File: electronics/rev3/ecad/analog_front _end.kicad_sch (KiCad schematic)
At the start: 20 parts, among them J3 Red Banana Plug, J4 Black Banana Plug, SW3 GF-161-0005, U10 MCP3561, U3 OPA4388IDR

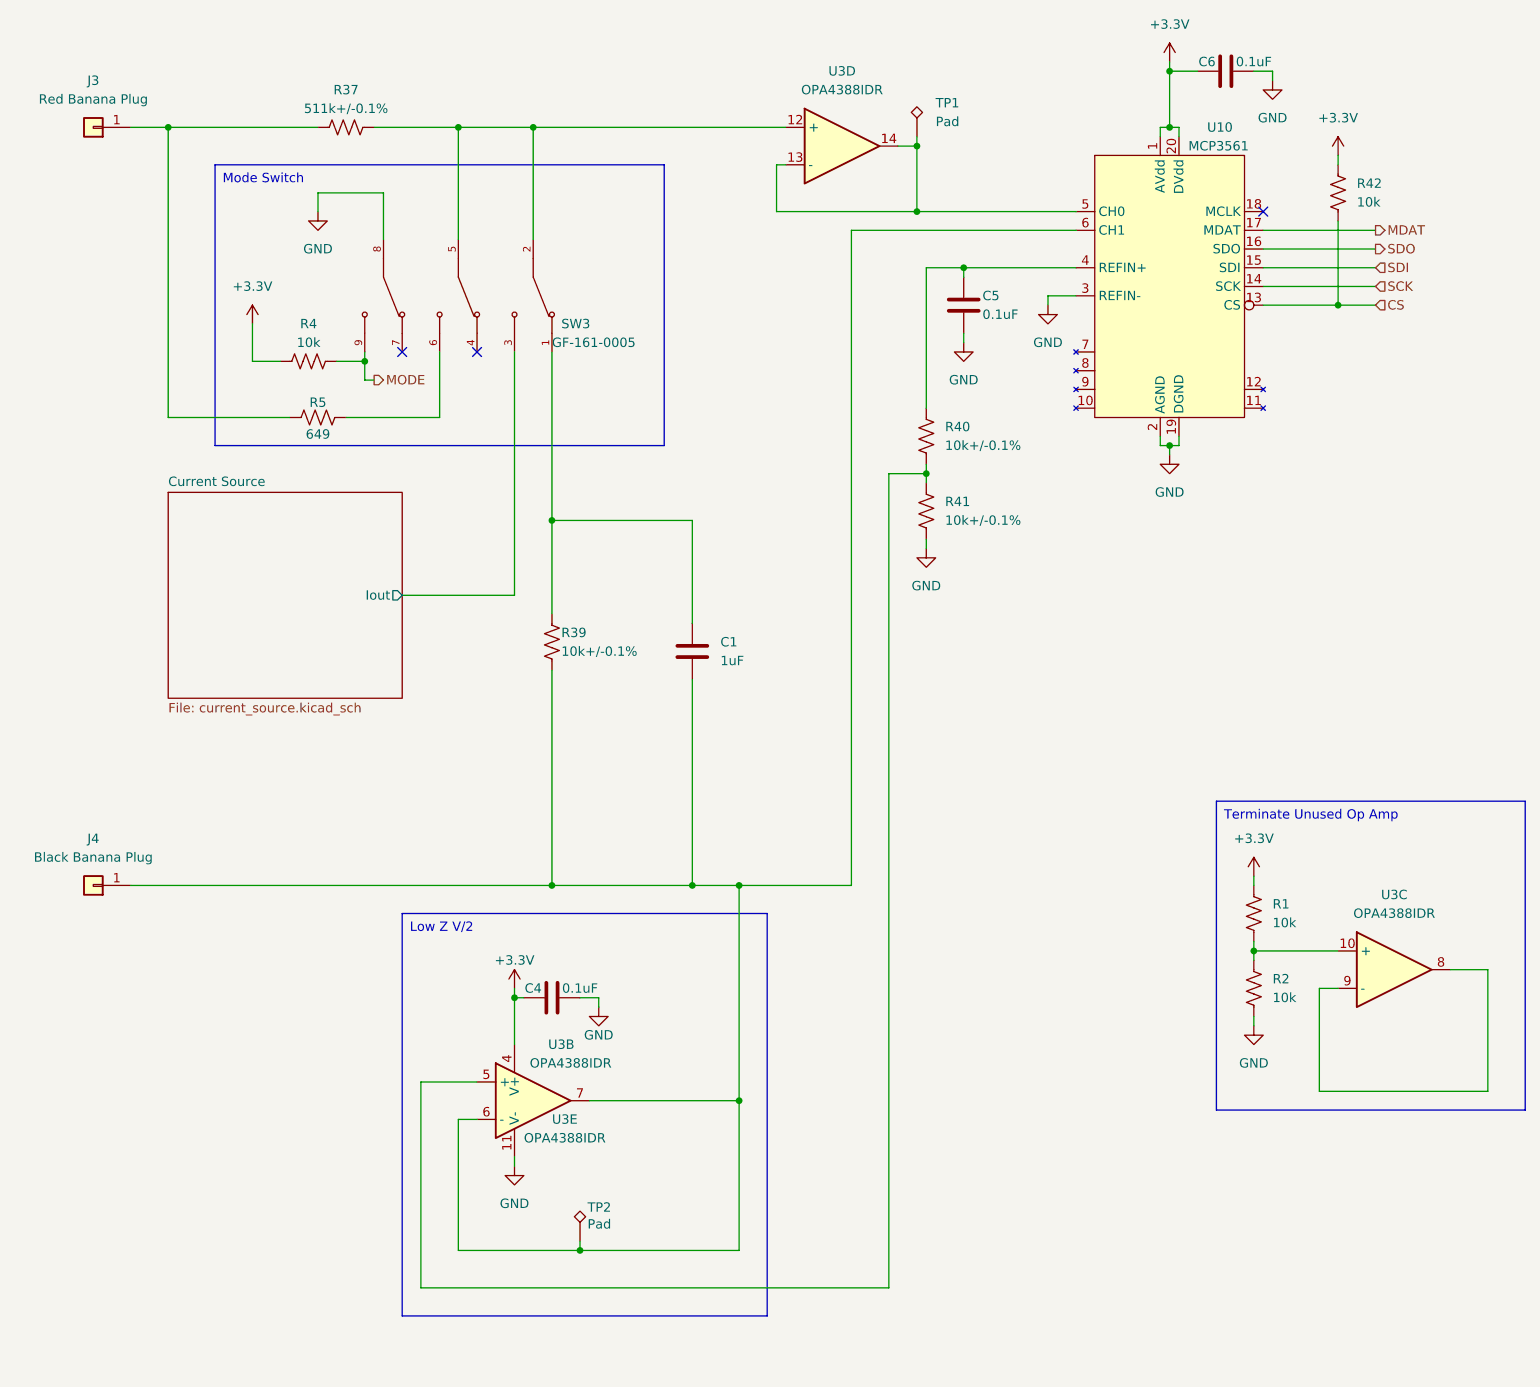
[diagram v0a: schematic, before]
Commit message: rev3 schematic work
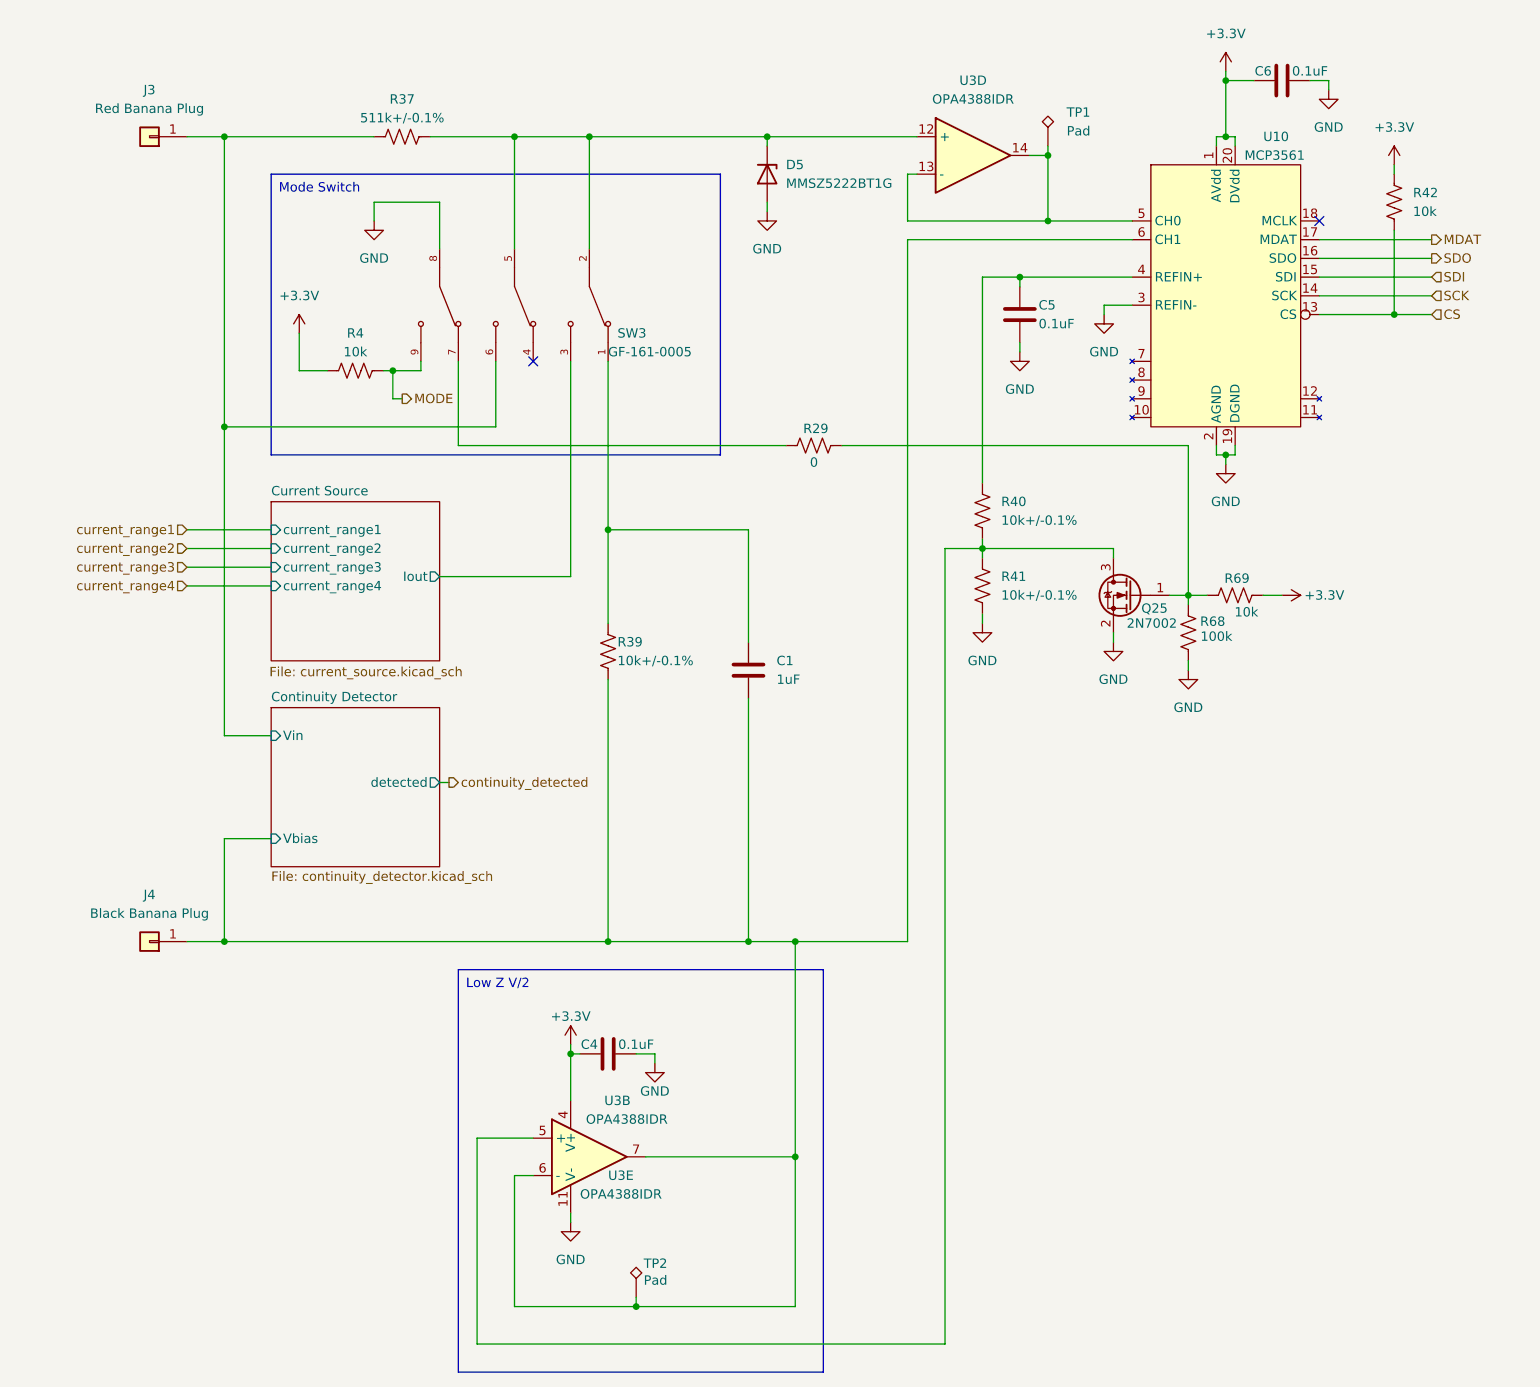
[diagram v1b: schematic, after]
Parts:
- removed R1, R2: 10k, Resistor_SMD:R_0805_2012Metric_Pad1.20x1.40mm_HandSolder, symbol Device:R_US
- removed R5: 649, Resistor_SMD:R_0805_2012Metric_Pad1.20x1.40mm_HandSolder, symbol Device:R_US
- removed unit 3 of U3
- added D5: MMSZ5222BT1G, symbol Device:D_Zener
- added Q25: 2N7002, Package_TO_SOT_SMD:SOT-23, symbol Transistor_FET:2N7002
- added R29: 0, symbol Device:R_US
- added R68: 100k, Resistor_SMD:R_0805_2012Metric, symbol Device:R_US
- added R69: 10k, symbol Device:R_US
- C1: footprint (none) -> Capacitor_SMD:C_0805_2012Metric
- U3: footprint Package_SO:SOIC-14_3.9x8.7mm_P1.27mm -> (none); Digikey Part # 296-53511-1-ND -> (none); Part # OPA4388IDR -> (none); Unit Price 4.92 -> (none)
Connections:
- net +3.3V: now also R69.2
- net GND: now also D5.2 (A), Q25.2 (S), R68.1
- net Continuity Detector/Vin: now reaches J3.1 (Pin_1), R37.1
- net Continuity Detector/Vin: now also SW3.6
- net Continuity Detector/Vbias: now reaches C1.2, J4.1 (Pin_1), R39.2, TP2.1, U10.6 (CH1), U3.6 (-), U3.7
- net at R40.2, R41.1, U3.5 (+): now also Q25.3 (D)
- net at R37.2, SW3.2, SW3.5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: now also D5.1 (K)
- net at SW3.7: now also R29.1
- new net: Q25.1 (G), R29.2, R68.2, R69.1
- no-connect marks 3 -> 2
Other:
- added sheet Continuity Detector (continuity_detector.kicad_sch)
- sheet Current Source ports: added current_range1, current_range2, current_range3, current_range4; removed none
- moved on the sheet: C1, C4, C5, C6, J3, J4, R37, R39, R4, R40, R41, R42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

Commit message: layout work rev3
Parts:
- D5: footprint (none) -> Diode_SMD:D_SOD-123
- R29, R69: footprint (none) -> Resistor_SMD:R_0805_2012Metric
- R37, R39, R4, R40, R41, R42: footprint Resistor_SMD:R_0805_2012Metric_Pad1.20x1.40mm_HandSolder -> Resistor_SMD:R_0805_2012Metric
- U3: footprint (none) -> Package_SO:SOIC-14_3.9x8.7mm_P1.27mm
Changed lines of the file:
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@@
 			)
 		)
-		(property "Footprint" ""
+		(property "Footprint" "Diode_SMD:D_SOD-123"
 			(at 133.35 35.56 0)
 			(effects
@@
 			)
 		)
-		(property "Footprint" "Resistor_SMD:R_0805_2012Metric_Pad1.20x1.40mm_HandSolder"
+		(property "Footprint" "Resistor_SMD:R_0805_2012Metric"
 			(at 163.576 81.534 90)
 			(effects
@@
 			)
 		)
-		(property "Footprint" "Resistor_SMD:R_0805_2012Metric_Pad1.20x1.40mm_HandSolder"
+		(property "Footprint" "Resistor_SMD:R_0805_2012Metric"
 			(at 219.456 39.624 90)
 			(effects
@@
 			)
 		)
-		(property "Footprint" "Resistor_SMD:R_0805_2012Metric_Pad1.20x1.40mm_HandSolder"
+		(property "Footprint" "Resistor_SMD:R_0805_2012Metric"
 			(at 77.724 61.214 90)
 			(effects
@@
 			)
 		)
-		(property "Footprint" "Resistor_SMD:R_0805_2012Metric_Pad1.20x1.40mm_HandSolder"
+		(property "Footprint" "Resistor_SMD:R_0805_2012Metric"
 			(at 112.776 100.584 90)
 			(effects
@@
 			)
 		)
-		(property "Footprint" "Resistor_SMD:R_0805_2012Metric_Pad1.20x1.40mm_HandSolder"
+		(property "Footprint" "Resistor_SMD:R_0805_2012Metric"
 			(at 84.074 29.464 90)
 			(effects
@@
 			)
 		)
-		(property "Footprint" ""
+		(property "Footprint" "Package_SO:SOIC-14_3.9x8.7mm_P1.27mm"
 			(at 161.29 33.02 0)
 			(effects
@@
 			)
 		)
-		(property "Footprint" ""
+		(property "Footprint" "Resistor_SMD:R_0805_2012Metric"
 			(at 197.104 91.694 90)
 			(effects
@@
 			)
 		)
-		(property "Footprint" ""
+		(property "Footprint" "Package_SO:SOIC-14_3.9x8.7mm_P1.27mm"
 			(at 109.22 168.91 0)
 			(effects
@@
 			)
 		)
-		(property "Footprint" ""
+		(property "Footprint" "Package_SO:SOIC-14_3.9x8.7mm_P1.27mm"
 			(at 109.22 168.91 0)
 			(effects
@@
 			)
 		)
-		(property "Footprint" "Resistor_SMD:R_0805_2012Metric_Pad1.20x1.40mm_HandSolder"
+		(property "Footprint" "Resistor_SMD:R_0805_2012Metric"
 			(at 163.576 91.694 90)
 			(effects
@@
 			)
 		)
-		(property "Footprint" ""
+		(property "Footprint" "Resistor_SMD:R_0805_2012Metric"
 			(at 139.954 71.374 90)
 			(effects

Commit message: layout complete
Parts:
- Q25: Digikey Part # (none) -> 2N7002NCT-ND; Part # (none) -> 2N7002; Unit Price (none) -> 0.45
- R69: Digikey Part # (none) -> RMCF0805FT10K0CT-ND; Part # (none) -> RMCF0805FT10K0; Unit Price (none) -> 0.1
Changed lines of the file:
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@@
+			)
+		)
+		(property "Digikey Part #" "2N7002NCT-ND"
+			(at 182.88 92.71 0)
+			(effects
+				(font
+					(size 1.27 1.27)
+				)
+				(hide yes)
+			)
+		)
+		(property "Part #" "2N7002"
+			(at 182.88 92.71 0)
+			(effects
+				(font
+					(size 1.27 1.27)
+				)
+				(hide yes)
+			)
+		)
+		(property "Unit Price" "0.45"
+			(at 182.88 92.71 0)
+			(effects
+				(font
+					(size 1.27 1.27)
+				)
+				(hide yes)
 			)
 		)
@@
 			(at 196.85 92.71 0)
 			(effects
+				(font
+					(size 1.27 1.27)
+				)
+				(hide yes)
+			)
+		)
+		(property "Digikey Part #" "RMCF0805FT10K0CT-ND"
+			(at 196.85 92.71 0)
+			(effects
+				(font
+					(size 1.27 1.27)
+				)
+				(hide yes)
+			)
+		)
+		(property "Part #" "RMCF0805FT10K0"
+			(at 196.85 92.71 0)
+			(effects
+				(font
+					(size 1.27 1.27)
+				)
+				(hide yes)
+			)
+		)
+		(property "Unit Price" "0.1"
+			(at 196.85 92.71 0)
+			(effects

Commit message: rev3 work
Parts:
- D5: value MMSZ5222BT1G -> DDZ9684-7
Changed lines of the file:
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@@
 			)
 		)
-		(property "Value" "MMSZ5222BT1G"
+		(property "Value" "DDZ9684-7"
 			(at 135.89 36.8299 90)
 			(effects

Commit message: BOM
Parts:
- C1: value 1uF -> 0.1uF; Digikey Part # (none) -> 1276-1003-1-ND; Part # (none) -> CL21B104KBCNNNC; Unit Price (none) -> 0.1
- D5: Digikey Part # (none) -> DDZ9684-7DICT-ND; Part # (none) -> DDZ9684-7; Unit Price (none) -> 0.1
- R29: Digikey Part # (none) -> 541-0.0ACT-ND; Part # (none) -> CRCW08050000Z0EA; Unit Price (none) -> 0.1
- R37: value 511k+/-0.1% -> 5.11M+/-1%; Digikey Part # P511KDACT-ND -> 541-5.11MCCT-ND; Part # ERA-6AEB5113V -> CRCW08055M11FKEA; Unit Price 0.13 -> 0.1
- R39: value 10k+/-0.1% -> 100k+/-0.1%
- R68: value 100k -> 100k+/-0.1%; Digikey Part # (none) -> P10KDACT-ND; Part # (none) -> ERA-6AEB103V; Unit Price (none) -> 0.13
- U3: Digikey Part # (none) -> 296-53511-1-ND; Part # (none) -> OPA4388IDR; Unit Price (none) -> 4.92
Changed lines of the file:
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@@
 			)
 		)
-		(property "Value" "1uF"
+		(property "Value" "0.1uF"
 			(at 134.62 104.1399 0)
 			(effects
@@
 		)
 		(property "Description" "Unpolarized capacitor"
+			(at 130.81 102.87 0)
+			(effects
+				(font
+					(size 1.27 1.27)
+				)
+				(hide yes)
+			)
+		)
+		(property "Digikey Part #" "1276-1003-1-ND"
+			(at 130.81 102.87 0)
+			(effects
+				(font
+					(size 1.27 1.27)
+				)
+				(hide yes)
+			)
+		)
+		(property "Part #" "CL21B104KBCNNNC"
+			(at 130.81 102.87 0)
+			(effects
+				(font
+					(size 1.27 1.27)
+				)
+				(hide yes)
+			)
+		)
+		(property "Unit Price" "0.1"
 			(at 130.81 102.87 0)
 			(effects
@@
 			)
 		)
+		(property "Digikey Part #" "DDZ9684-7DICT-ND"
+			(at 133.35 35.56 0)
+			(effects
+				(font
+					(size 1.27 1.27)
+				)
+				(hide yes)
+			)
+		)
+		(property "Part #" "DDZ9684-7"
+			(at 133.35 35.56 0)
+			(effects
+				(font
+					(size 1.27 1.27)
+				)
+				(hide yes)
+			)
+		)
+		(property "Unit Price" "0.1"
+			(at 133.35 35.56 0)
+			(effects
+				(font
+					(size 1.27 1.27)
+				)
+				(hide yes)
+			)
+		)
 		(pin "1"
 		)
@@
 			)
 		)
-		(property "Value" "10k+/-0.1%"
+		(property "Value" "100k+/-0.1%"
 			(at 113.03 101.6 0)
 			(effects
@@
 			)
 		)
-		(property "Value" "100k"
-			(at 194.31 98.298 0)
+		(property "Value" "100k+/-0.1%"
+			(at 198.882 98.552 0)
 			(effects
 				(font
@@
 		)
 		(property "Description" "Resistor, US symbol"
+			(at 190.5 97.79 0)
+			(effects
+				(font
+					(size 1.27 1.27)
+				)
+				(hide yes)
+			)
+		)
+		(property "Digikey Part #" "P10KDACT-ND"
+			(at 190.5 97.79 0)
+			(effects
+				(font
+					(size 1.27 1.27)
+				)
+				(hide yes)
+			)
+		)
+		(property "Part #" "ERA-6AEB103V"
+			(at 190.5 97.79 0)
+			(effects
+				(font
+					(size 1.27 1.27)
+				)
+				(hide yes)
+			)
+		)
+		(property "Unit Price" "0.13"
 			(at 190.5 97.79 0)
 			(effects
@@
 			)
 		)
-		(property "Value" "511k+/-0.1%"
+		(property "Value" "5.11M+/-1%"
 			(at 83.82 27.94 90)
 			(effects
@@
 			)
 		)
-		(property "Digikey Part #" "P511KDACT-ND"
+		(property "Digikey Part #" "541-5.11MCCT-ND"
 			(at 83.82 30.48 0)
 			(effects
@@
 			)
 		)
-		(property "Part #" "ERA-6AEB5113V"
+		(property "Part #" "CRCW08055M11FKEA"
 			(at 83.82 30.48 0)
 			(effects
@@
 			)
 		)
-		(property "Unit Price" "0.13"
+		(property "Unit Price" "0.1"
 			(at 83.82 30.48 0)
 			(effects
@@
 			)
 		)
+		(property "Digikey Part #" "296-53511-1-ND"
+			(at 161.29 33.02 0)
+			(effects
+				(font
+					(size 1.27 1.27)
+				)
+				(hide yes)
+			)
+		)
+		(property "Part #" "OPA4388IDR"
+			(at 161.29 33.02 0)
+			(effects
+				(font
+					(size 1.27 1.27)
+				)
+				(hide yes)
+			)
+		)
+		(property "Unit Price" "4.92"
+			(at 161.29 33.02 0)
+			(effects
+				(font
+					(size 1.27 1.27)
+				)
+				(hide yes)
+			)
+		)
 		(pin "1"
 		)
@@
 			)
 		)
+		(property "Digikey Part #" "296-53511-1-ND"
+			(at 109.22 168.91 0)
+			(effects
+				(font
+					(size 1.27 1.27)
+				)
+				(hide yes)
+			)
+		)
+		(property "Part #" "OPA4388IDR"
+			(at 109.22 168.91 0)
+			(effects
+				(font
+					(size 1.27 1.27)
+				)
+				(hide yes)
+			)
+		)
+		(property "Unit Price" "4.92"
+			(at 109.22 168.91 0)
+			(effects
+				(font
+					(size 1.27 1.27)
+				)
+				(hide yes)
+			)
+		)
 		(pin "1"
 		)
@@
 			)
 		)
+		(property "Digikey Part #" "296-53511-1-ND"
+			(at 109.22 168.91 0)
+			(effects
+				(font
+					(size 1.27 1.27)
+				)
+				(hide yes)
+			)
+		)
+		(property "Part #" "OPA4388IDR"
+			(at 109.22 168.91 0)
+			(effects
+				(font
+					(size 1.27 1.27)
+				)
+				(hide yes)
+			)
+		)
+		(property "Unit Price" "4.92"
+			(at 109.22 168.91 0)
+			(effects
+				(font
+					(size 1.27 1.27)
+				)
+				(hide yes)
+			)
+		)
 		(pin "1"
 		)
@@
 			(at 139.7 72.39 0)
 			(effects
+				(font
+					(size 1.27 1.27)
+				)
+				(hide yes)
+			)
+		)
+		(property "Digikey Part #" "541-0.0ACT-ND"
+			(at 139.7 72.39 0)
+			(effects
+				(font
+					(size 1.27 1.27)
+				)
+				(hide yes)
+			)
+		)
+		(property "Part #" "CRCW08050000Z0EA"
+			(at 139.7 72.39 0)
+			(effects
+				(font
+					(size 1.27 1.27)
+				)
+				(hide yes)
+			)
+		)
+		(property "Unit Price" "0.1"
+			(at 139.7 72.39 0)
+			(effects
